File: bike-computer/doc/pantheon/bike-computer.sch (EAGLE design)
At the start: 19 parts, among them Q1 BSS92, Q2 BSS92, T1 BC547, T2 BC547, T3 BC547

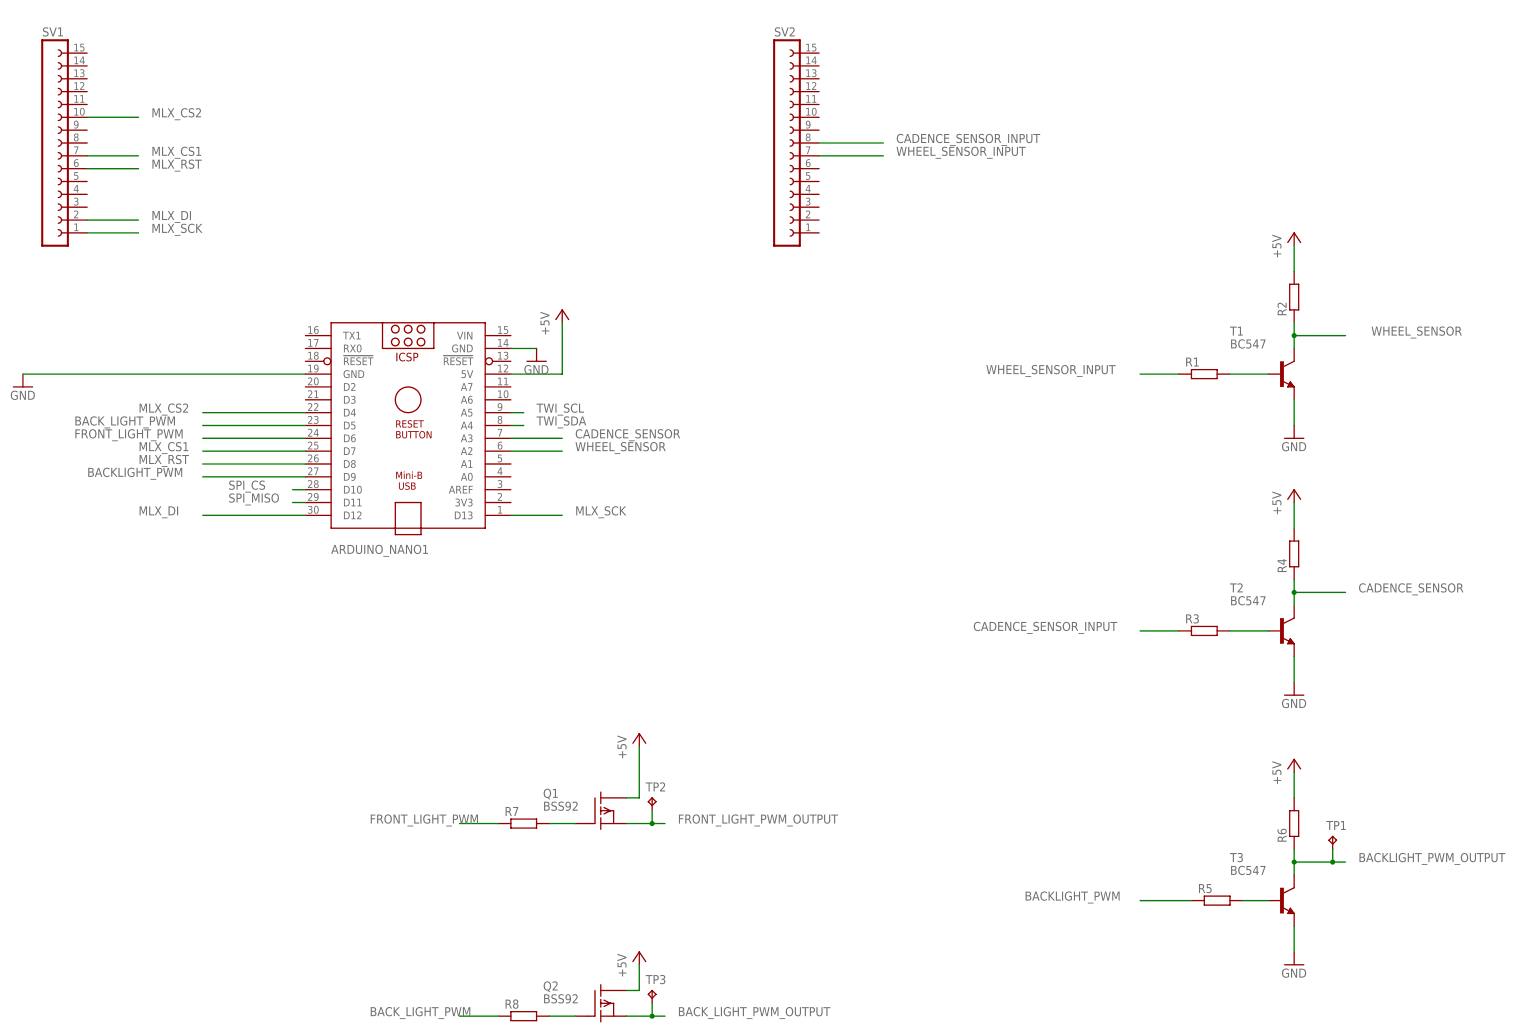
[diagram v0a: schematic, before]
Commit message: [Bike] Simplify speed and cadence sensors circuits.
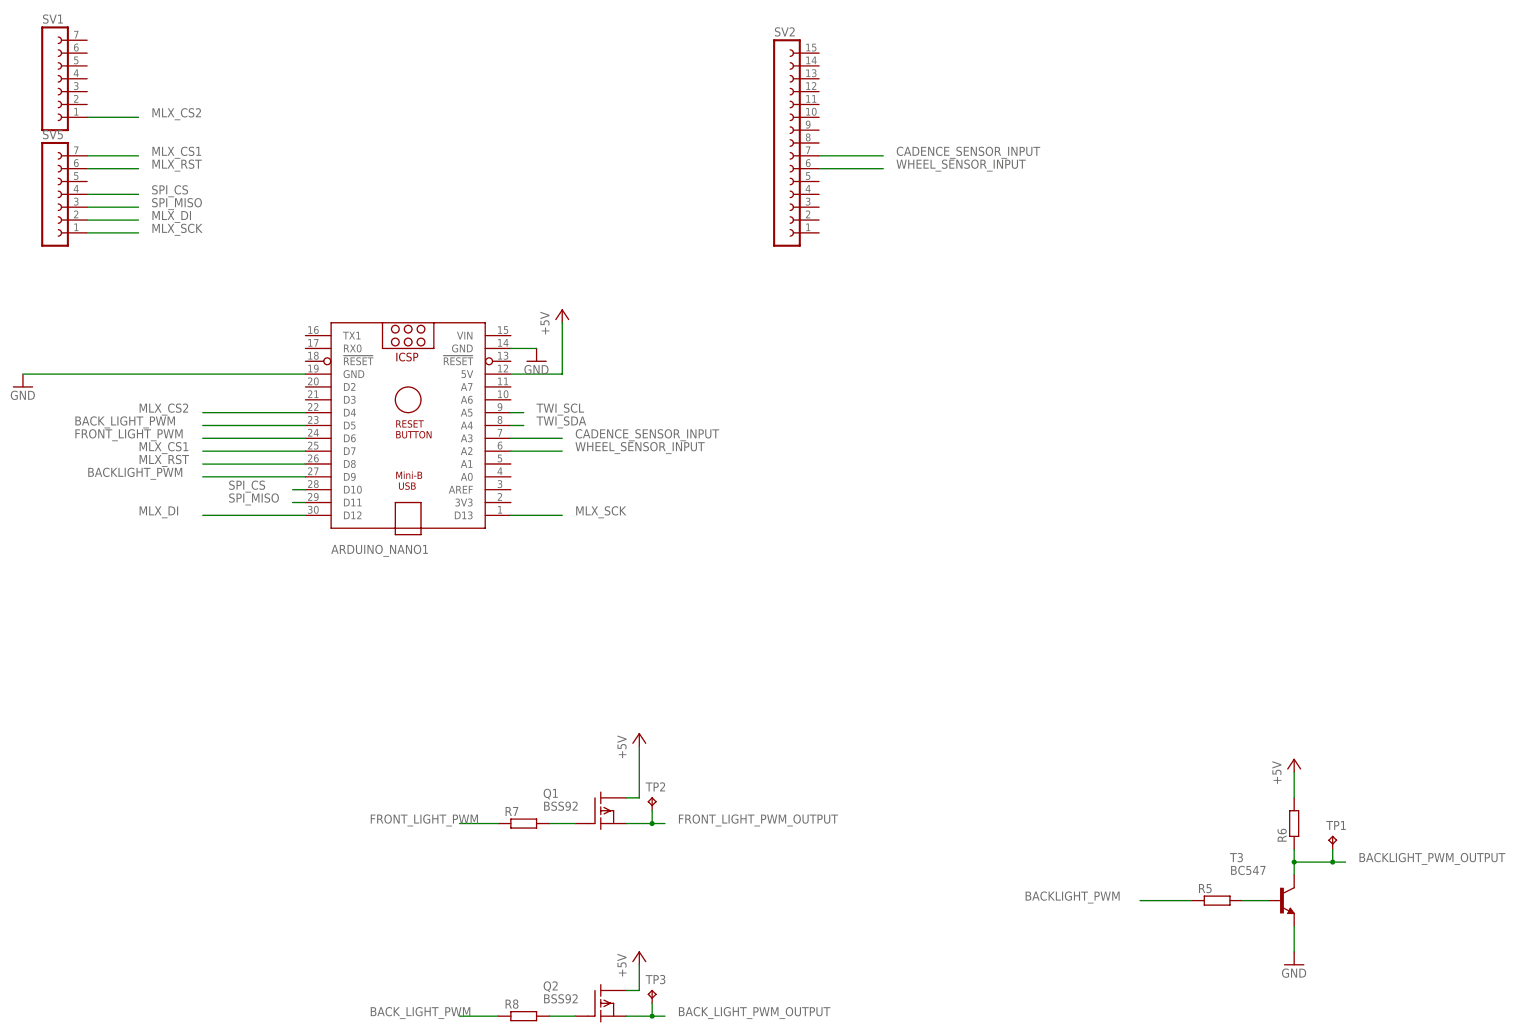
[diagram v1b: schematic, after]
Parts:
- removed R1, R2, R3, R4: (no value), rcl:R-EU_0204/5
- removed T1, T2: BC547, transistor:BC547
- added SV5: (no value), con-lsta:FE07-1
- R7, R8: device rcl:R-EU_0204/5 -> rcl:R-EU_0204/7
- SV1: device con-lsta:FE15-1 -> con-lsta:FE07-1
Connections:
- removed net CADENCE_SENSOR: ARDUINO_NANO1.A3, R4.1, T2.C
- removed net N$1: R1.2, T1.B
- removed net N$3: R3.2, T2.B
- removed net WHEEL_SENSOR: ARDUINO_NANO1.A2, R2.1, T1.C
- net +5V: no longer R2.2, R4.2
- net CADENCE_SENSOR_INPUT: now also ARDUINO_NANO1.A3, SV2.7; no longer R3.1, SV2.8
- net GND: no longer T1.E, T2.E
- net MLX_CS1: now also SV5.7; no longer SV1.7
- net MLX_CS2: now also SV1.1; no longer SV1.10
- net MLX_DI: now also SV5.2; no longer SV1.2
- net MLX_RST: now also SV5.6; no longer SV1.6
- net MLX_SCK: now also SV5.1; no longer SV1.1
- net SPI_CS: now also SV5.4
- net SPI_MISO: now also SV5.3
- net WHEEL_SENSOR_INPUT: now also ARDUINO_NANO1.A2, SV2.6; no longer R1.1, SV2.7

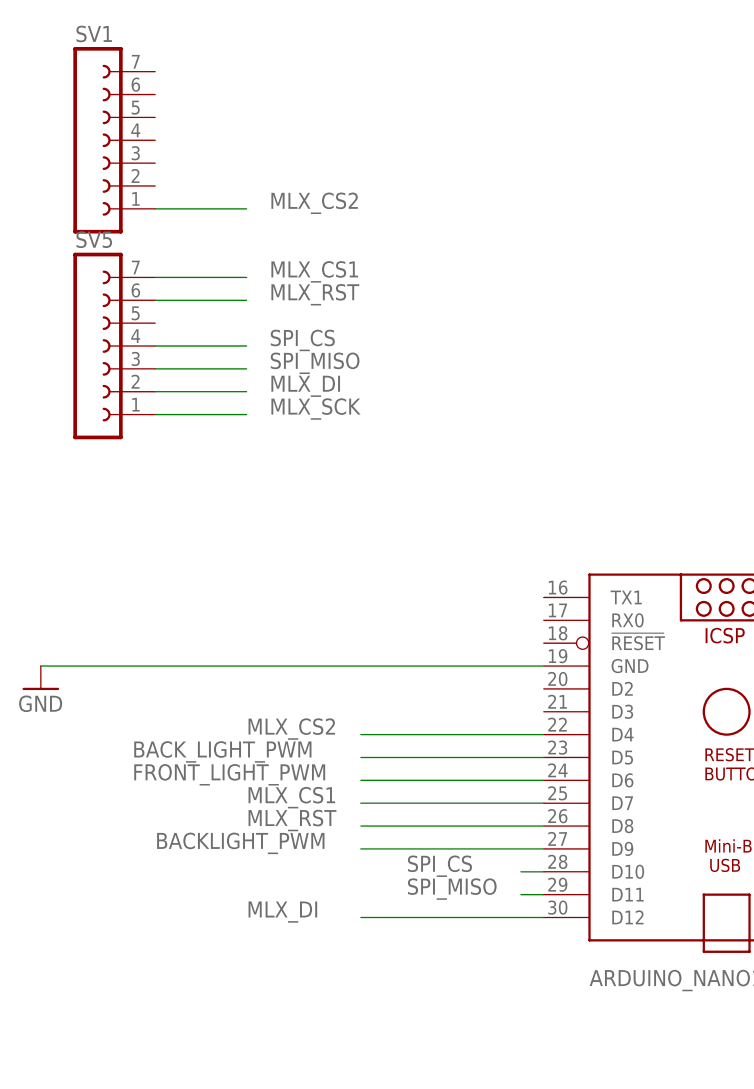
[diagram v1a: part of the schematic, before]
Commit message: [Bike] Bugfix: swapped MISO and MOSI.
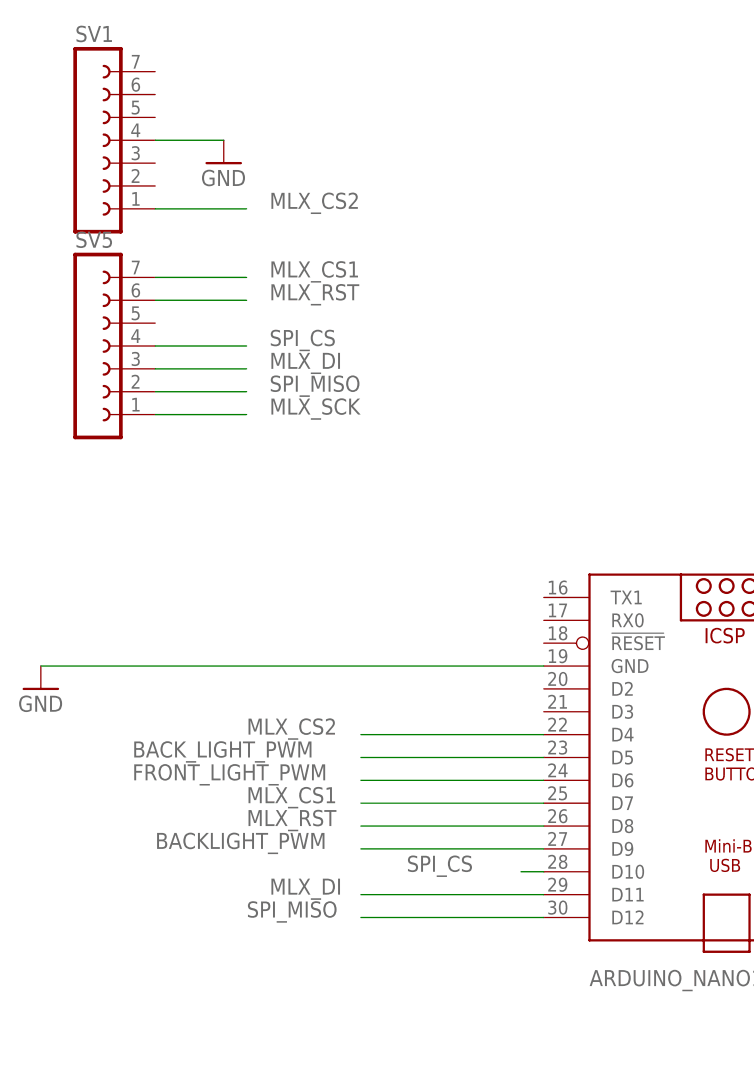
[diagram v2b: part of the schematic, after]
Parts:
- R6: device rcl:R-EU_0204/5 -> rcl:R-EU_0207/10
- R7, R8: device rcl:R-EU_0204/7 -> rcl:R-EU_0204/5
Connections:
- net GND: now also SV1.4
- net MLX_DI: now also ARDUINO_NANO1.D11, SV5.3; no longer ARDUINO_NANO1.D12, SV5.2
- net SPI_MISO: now also ARDUINO_NANO1.D12, SV5.2; no longer ARDUINO_NANO1.D11, SV5.3
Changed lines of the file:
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@@
 <grid distance="0.1" unitdist="inch" unit="inch" style="lines" multiple="1" display="no" altdistance="0.01" altunitdist="inch" altunit="inch"/>
 <layers>
-<layer number="1" name="Top" color="4" fill="1" visible="yes" active="no"/>
-<layer number="16" name="Bottom" color="1" fill="1" visible="yes" active="no"/>
-<layer number="17" name="Pads" color="2" fill="1" visible="yes" active="no"/>
-<layer number="18" name="Vias" color="2" fill="1" visible="yes" active="no"/>
-<layer number="19" name="Unrouted" color="6" fill="1" visible="yes" active="no"/>
-<layer number="20" name="Dimension" color="24" fill="1" visible="yes" active="no"/>
-<layer number="21" name="tPlace" color="7" fill="1" visible="yes" active="no"/>
-<layer number="22" name="bPlace" color="7" fill="1" visible="yes" active="no"/>
-<layer number="23" name="tOrigins" color="15" fill="1" visible="yes" active="no"/>
-<layer number="24" name="bOrigins" color="15" fill="1" visible="yes" active="no"/>
-<layer number="25" name="tNames" color="7" fill="1" visible="yes" active="no"/>
-<layer number="26" name="bNames" color="7" fill="1" visible="yes" active="no"/>
-<layer number="27" name="tValues" color="7" fill="1" visible="yes" active="no"/>
-<layer number="28" name="bValues" color="7" fill="1" visible="yes" active="no"/>
+<layer number="1" name="Top" color="4" fill="1" visible="no" active="no"/>
+<layer number="16" name="Bottom" color="1" fill="1" visible="no" active="no"/>
+<layer number="17" name="Pads" color="2" fill="1" visible="no" active="no"/>
+<layer number="18" name="Vias" color="2" fill="1" visible="no" active="no"/>
+<layer number="19" name="Unrouted" color="6" fill="1" visible="no" active="no"/>
+<layer number="20" name="Dimension" color="24" fill="1" visible="no" active="no"/>
+<layer number="21" name="tPlace" color="7" fill="1" visible="no" active="no"/>
+<layer number="22" name="bPlace" color="7" fill="1" visible="no" active="no"/>
+<layer number="23" name="tOrigins" color="15" fill="1" visible="no" active="no"/>
+<layer number="24" name="bOrigins" color="15" fill="1" visible="no" active="no"/>
+<layer number="25" name="tNames" color="7" fill="1" visible="no" active="no"/>
+<layer number="26" name="bNames" color="7" fill="1" visible="no" active="no"/>
+<layer number="27" name="tValues" color="7" fill="1" visible="no" active="no"/>
+<layer number="28" name="bValues" color="7" fill="1" visible="no" active="no"/>
 <layer number="29" name="tStop" color="7" fill="3" visible="no" active="no"/>
 <layer number="30" name="bStop" color="7" fill="6" visible="no" active="no"/>
@@
 <layer number="35" name="tGlue" color="7" fill="4" visible="no" active="no"/>
 <layer number="36" name="bGlue" color="7" fill="5" visible="no" active="no"/>
-<layer number="37" name="tTest" color="7" fill="1" visible="yes" active="no"/>
-<layer number="38" name="bTest" color="7" fill="1" visible="yes" active="no"/>
+<layer number="37" name="tTest" color="7" fill="1" visible="no" active="no"/>
+<layer number="38" name="bTest" color="7" fill="1" visible="no" active="no"/>
 <layer number="39" name="tKeepout" color="4" fill="11" visible="no" active="no"/>
 <layer number="40" name="bKeepout" color="1" fill="11" visible="no" active="no"/>
@@
 <layer number="44" name="Drills" color="7" fill="1" visible="no" active="no"/>
 <layer number="45" name="Holes" color="7" fill="1" visible="no" active="no"/>
-<layer number="46" name="Milling" color="3" fill="1" visible="yes" active="no"/>
-<layer number="47" name="Measures" color="7" fill="1" visible="yes" active="no"/>
-<layer number="48" name="Document" color="7" fill="1" visible="yes" active="no"/>
-<layer number="49" name="Reference" color="7" fill="1" visible="yes" active="no"/>
-<layer number="51" name="tDocu" color="7" fill="1" visible="yes" active="no"/>
-<layer number="52" name="bDocu" color="7" fill="1" visible="yes" active="no"/>
+<layer number="46" name="Milling" color="3" fill="1" visible="no" active="no"/>
+<layer number="47" name="Measures" color="7" fill="1" visible="no" active="no"/>
+<layer number="48" name="Document" color="7" fill="1" visible="no" active="no"/>
+<layer number="49" name="Reference" color="7" fill="1" visible="no" active="no"/>
+<layer number="51" name="tDocu" color="7" fill="1" visible="no" active="no"/>
+<layer number="52" name="bDocu" color="7" fill="1" visible="no" active="no"/>
 <layer number="88" name="SimResults" color="9" fill="1" visible="yes" active="yes"/>
 <layer number="89" name="SimProbes" color="9" fill="1" visible="yes" active="yes"/>
@@
 <part name="T3" library="transistor" library_urn="urn:adsk.eagle:library:402" deviceset="BC547" device="" package3d_urn="urn:adsk.eagle:package:28523/2"/>
 <part name="R5" library="rcl" library_urn="urn:adsk.eagle:library:334" deviceset="R-EU_" device="0204/5" package3d_urn="urn:adsk.eagle:package:23488/1"/>
-<part name="R6" library="rcl" library_urn="urn:adsk.eagle:library:334" deviceset="R-EU_" device="0204/5" package3d_urn="urn:adsk.eagle:package:23488/1"/>
-<part name="R7" library="rcl" library_urn="urn:adsk.eagle:library:334" deviceset="R-EU_" device="0204/7" package3d_urn="urn:adsk.eagle:package:23498/2"/>
-<part name="R8" library="rcl" library_urn="urn:adsk.eagle:library:334" deviceset="R-EU_" device="0204/7" package3d_urn="urn:adsk.eagle:package:23498/2"/>
+<part name="R6" library="rcl" library_urn="urn:adsk.eagle:library:334" deviceset="R-EU_" device="0207/10" package3d_urn="urn:adsk.eagle:package:23491/2"/>
+<part name="R7" library="rcl" library_urn="urn:adsk.eagle:library:334" deviceset="R-EU_" device="0204/5" package3d_urn="urn:adsk.eagle:package:23488/1"/>
+<part name="R8" library="rcl" library_urn="urn:adsk.eagle:library:334" deviceset="R-EU_" device="0204/5" package3d_urn="urn:adsk.eagle:package:23488/1"/>
 <part name="Q1" library="transistor-fet" library_urn="urn:adsk.eagle:library:396" deviceset="BSS92" device="" package3d_urn="urn:adsk.eagle:package:28523/2"/>
 <part name="Q2" library="transistor-fet" library_urn="urn:adsk.eagle:library:396" deviceset="BSS92" device="" package3d_urn="urn:adsk.eagle:package:28523/2"/>
@@
 <part name="SV1" library="con-lsta" library_urn="urn:adsk.eagle:library:161" deviceset="FE07-1" device="" package3d_urn="urn:adsk.eagle:package:8223/1"/>
 <part name="SV5" library="con-lsta" library_urn="urn:adsk.eagle:library:161" deviceset="FE07-1" device="" package3d_urn="urn:adsk.eagle:package:8223/1"/>
+<part name="GND2" library="supply1" library_urn="urn:adsk.eagle:library:371" deviceset="GND" device=""/>
 </parts>
 <sheets>
@@
 <attribute name="NAME" x="-3.81" y="104.902" size="1.778" layer="95"/>
 </instance>
+<instance part="GND2" gate="1" x="12.7" y="114.3" smashed="yes">
+<attribute name="VALUE" x="10.16" y="111.76" size="1.778" layer="96"/>
+</instance>
 </instances>
 <busses>
@@
 <net name="MLX_DI" class="0">
 <segment>
-<pinref part="ARDUINO_NANO1" gate="G$1" pin="D12"/>
-<wire x1="48.26" y1="30.48" x2="27.94" y2="30.48" width="0.1524" layer="91"/>
-<label x="15.24" y="30.48" size="1.778" layer="95"/>
-</segment>
-<segment>
-<wire x1="5.08" y1="88.9" x2="15.24" y2="88.9" width="0.1524" layer="91"/>
-<pinref part="SV5" gate="G$1" pin="2"/>
-<label x="17.78" y="88.9" size="1.778" layer="95"/>
+<label x="17.78" y="33.02" size="1.778" layer="95"/>
+<pinref part="ARDUINO_NANO1" gate="G$1" pin="D11"/>
+<wire x1="27.94" y1="33.02" x2="48.26" y2="33.02" width="0.1524" layer="91"/>
+</segment>
+<segment>
+<label x="17.78" y="91.44" size="1.778" layer="95"/>
+<pinref part="SV5" gate="G$1" pin="3"/>
+<wire x1="15.24" y1="91.44" x2="5.08" y2="91.44" width="0.1524" layer="91"/>
 </segment>
 </net>
@@
 <pinref part="GND1" gate="1" pin="GND"/>
 <wire x1="88.9" y1="63.5" x2="93.98" y2="63.5" width="0.1524" layer="91"/>
+</segment>
+<segment>
+<pinref part="SV1" gate="G$1" pin="4"/>
+<pinref part="GND2" gate="1" pin="GND"/>
+<wire x1="5.08" y1="116.84" x2="12.7" y2="116.84" width="0.1524" layer="91"/>
 </segment>
 </net>
@@
 <net name="SPI_MISO" class="0">
 <segment>
-<pinref part="ARDUINO_NANO1" gate="G$1" pin="D11"/>
-<wire x1="48.26" y1="33.02" x2="45.72" y2="33.02" width="0.1524" layer="91"/>
-<label x="33.02" y="33.02" size="1.778" layer="95"/>
-</segment>
-<segment>
-<pinref part="SV5" gate="G$1" pin="3"/>
-<wire x1="5.08" y1="91.44" x2="15.24" y2="91.44" width="0.1524" layer="91"/>
-<label x="17.78" y="91.44" size="1.778" layer="95"/>
-</segment>
-</net>
+<pinref part="ARDUINO_NANO1" gate="G$1" pin="D12"/>
+<wire x1="48.26" y1="30.48" x2="27.94" y2="30.48" width="0.1524" layer="91"/>
+<label x="15.24" y="30.48" size="1.778" layer="95"/>
+</segment>
+<segment>
+<pinref part="SV5" gate="G$1" pin="2"/>
+<wire x1="5.08" y1="88.9" x2="15.24" y2="88.9" width="0.1524" layer="91"/>
+<label x="17.78" y="88.9" size="1.778" layer="95"/>
+</segment>
+</net>
